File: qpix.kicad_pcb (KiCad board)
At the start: 4 copper layers, 82.6 x 92.8 mm, 110 parts, among them J1 Conn_01x40, J10 VC, J11 Conn_Coaxial_Power, J13 DigReset, J2 Conn_01x09, J3 Conn_02x03, J4 Conn_02x03, J5 SPI, J6 Conn_02x03, J7 Conn_Coaxial, J8 Conn_02x03, J9 Conn_Coaxial_Power, Q1 AO7400, Q2 AO7400, Q3 AO7400, Q4 AO7400, U1 qpix_digital, U2 TPS73101DBV, U3 9DMV0141AKILF, U4 DS90C401M_NOPB

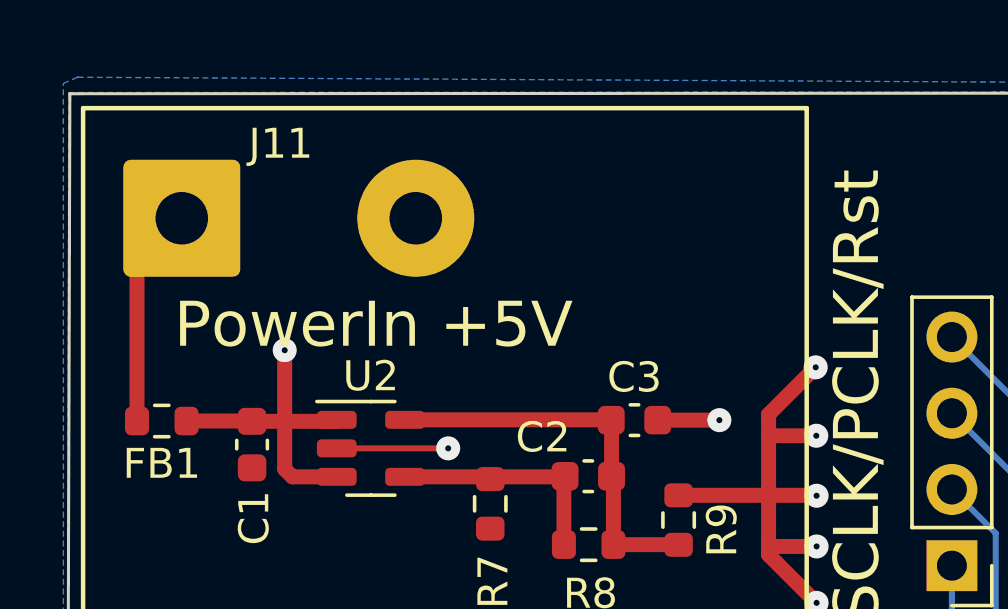
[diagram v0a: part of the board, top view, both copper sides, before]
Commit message: replace wire connector for 5V input with SMA conn
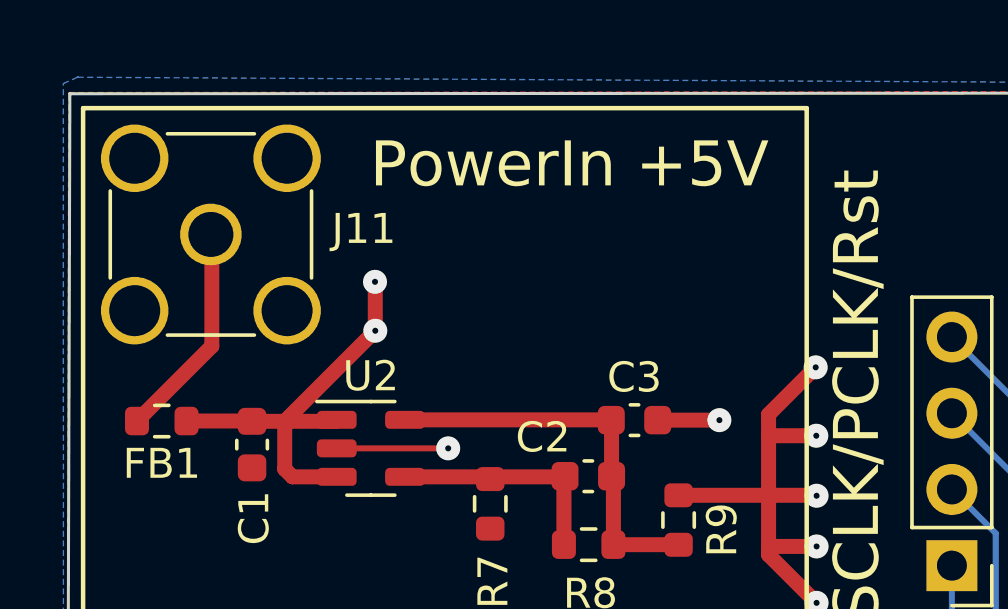
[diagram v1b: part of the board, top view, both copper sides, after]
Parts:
- J11: footprint Connector_Wire:SolderWire-1sqmm_1x02_P7.8mm_D1.4mm_OD3.9mm -> Connector_Coaxial:SMA_Amphenol_901-144_Vertical
- moved J11 1.11 mm to (100.2, 54.2)
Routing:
- net +5V: track 16.4 -> 19.9 mm, vias 5 -> 6
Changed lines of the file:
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@@
     )
   )
-  (footprint "Connector_Wire:SolderWire-1sqmm_1x02_P7.8mm_D1.4mm_OD3.9mm" (layer "F.Cu")
-    (at 99.26 53.62)
-    (descr "Soldered wire connection, for 2 times 1 mm² wires, reinforced insulation, conductor diameter 1.4mm, outer diameter 3.9mm, size source Multi-Contact FLEXI-xV 1.0 (https://ec.staubli.com/AcroFiles/Catalogues/TM_Cab-Main-11014119_(en)_hi.pdf), bend radius 3 times outer diameter, generated with kicad-footprint-generator")
-    (tags "connector wire 1sqmm")
+  (footprint "Connector_Coaxial:SMA_Amphenol_901-144_Vertical" (layer "F.Cu")
+    (at 100.23 54.16)
+    (descr "https://www.amphenolrf.com/downloads/dl/file/id/7023/product/3103/901_144_customer_drawing.pdf")
+    (tags "SMA THT Female Jack Vertical")
     (property "Sheetfile" "qpix-power.kicad_sch")
     (property "Sheetname" "qpix-power")
     (property "ki_description" "coaxial connector (BNC, SMA, SMB, SMC, Cinch/RCA, LEMO, ...)")
     (property "ki_keywords" "BNC SMA SMB SMC LEMO coaxial connector CINCH RCA")
-    (attr exclude_from_pos_files)
-    (fp_text reference "J11" (at 3.3 -2.48) (layer "F.SilkS")
+    (attr through_hole)
+    (fp_text reference "J11" (at 5.1 -0.18) (layer "F.SilkS")
         (effects (font (size 1 1) (thickness 0.15)))
     )
-    (fp_text value "Conn_Coaxial_Power" (at 3.9 3.15) (layer "F.Fab")
+    (fp_text value "Conn_Coaxial_Power" (at 0 5) (layer "F.Fab")
         (effects (font (size 1 1) (thickness 0.15)))
     )
-    (fp_text user "${REFERENCE}" (at 3.9 0 90) (layer "F.Fab")
+    (fp_text user "${REFERENCE}" (at 0 0) (layer "F.Fab")
         (effects (font (size 1 1) (thickness 0.15)))
     )
-    (fp_line (start -2.7 -2.45) (end -2.7 2.45)
-      (stroke (width 0.05) (type solid)) (layer "F.CrtYd"))
-    (fp_line (start -2.7 2.45) (end 2.7 2.45)
-      (stroke (width 0.05) (type solid)) (layer "F.CrtYd"))
-    (fp_line (start 2.7 -2.45) (end -2.7 -2.45)
-      (stroke (width 0.05) (type solid)) (layer "F.CrtYd"))
-    (fp_line (start 2.7 2.45) (end 2.7 -2.45)
-      (stroke (width 0.05) (type solid)) (layer "F.CrtYd"))
-    (fp_line (start 5.1 -2.45) (end 5.1 2.45)
+    (fp_line (start -3.355 -1.45) (end -3.355 1.45)
+      (stroke (width 0.12) (type solid)) (layer "F.SilkS"))
+    (fp_line (start -1.45 -3.355) (end 1.45 -3.355)
+      (stroke (width 0.12) (type solid)) (layer "F.SilkS"))
+    (fp_line (start -1.45 3.355) (end 1.45 3.355)
+      (stroke (width 0.12) (type solid)) (layer "F.SilkS"))
+    (fp_line (start 3.355 -1.45) (end 3.355 1.45)
+      (stroke (width 0.12) (type solid)) (layer "F.SilkS"))
+    (fp_line (start -4.17 -4.17) (end -4.17 4.17)
       (stroke (width 0.05) (type solid)) (layer "F.CrtYd"))
-    (fp_line (start 5.1 2.45) (end 10.5 2.45)
+    (fp_line (start -4.17 -4.17) (end 4.17 -4.17)
       (stroke (width 0.05) (type solid)) (layer "F.CrtYd"))
-    (fp_line (start 10.5 -2.45) (end 5.1 -2.45)
+    (fp_line (start 4.17 4.17) (end -4.17 4.17)
       (stroke (width 0.05) (type solid)) (layer "F.CrtYd"))
-    (fp_line (start 10.5 2.45) (end 10.5 -2.45)
+    (fp_line (start 4.17 4.17) (end 4.17 -4.17)
       (stroke (width 0.05) (type solid)) (layer "F.CrtYd"))
-    (fp_circle (center 0 0) (end 1.95 0)
-      (stroke (width 0.1) (type solid)) (fill none) (layer "F.Fab"))
-    (fp_circle (center 7.8 0) (end 9.75 0)
+    (fp_line (start -3.175 -3.175) (end -3.175 3.175)
+      (stroke (width 0.1) (type solid)) (layer "F.Fab"))
+    (fp_line (start -3.175 -3.175) (end 3.175 -3.175)
+      (stroke (width 0.1) (type solid)) (layer "F.Fab"))
+    (fp_line (start -3.175 3.175) (end 3.175 3.175)
+      (stroke (width 0.1) (type solid)) (layer "F.Fab"))
+    (fp_line (start 3.175 -3.175) (end 3.175 3.175)
+      (stroke (width 0.1) (type solid)) (layer "F.Fab"))
+    (fp_circle (center 0 0) (end 3.175 0)
       (stroke (width 0.1) (type solid)) (fill none) (layer "F.Fab"))
-    (pad "1" thru_hole roundrect (at 0 0) (size 3.9 3.9) (drill 1.75) (layers "*.Cu" "*.Mask") (roundrect_rratio 0.06410307692)
+    (pad "1" thru_hole circle (at 0 0) (size 2.05 2.05) (drill 1.5) (layers "*.Cu" "*.Mask")
       (net 71 "Net-(J11-In)") (pinfunction "In") (pintype "passive"))
-    (pad "2" thru_hole circle (at 7.8 0) (size 3.9 3.9) (drill 1.75) (layers "*.Cu" "*.Mask")
+    (pad "2" thru_hole circle (at -2.54 -2.54) (size 2.25 2.25) (drill 1.7) (layers "*.Cu" "*.Mask")
+      (net 80 "GND") (pinfunction "Ext") (pintype "passive"))
+    (pad "2" thru_hole circle (at -2.54 2.54) (size 2.25 2.25) (drill 1.7) (layers "*.Cu" "*.Mask")
+      (net 80 "GND") (pinfunction "Ext") (pintype "passive"))
+    (pad "2" thru_hole circle (at 2.54 -2.54) (size 2.25 2.25) (drill 1.7) (layers "*.Cu" "*.Mask")
+      (net 80 "GND") (pinfunction "Ext") (pintype "passive"))
+    (pad "2" thru_hole circle (at 2.54 2.54) (size 2.25 2.25) (drill 1.7) (layers "*.Cu" "*.Mask")
       (net 80 "GND") (pinfunction "Ext") (pintype "passive"))
-    (model "${KICAD6_3DMODEL_DIR}/Connector_Wire.3dshapes/SolderWire-1sqmm_1x02_P7.8mm_D1.4mm_OD3.9mm.wrl"
+    (model "${KICAD6_3DMODEL_DIR}/Connector_Coaxial.3dshapes/SMA_Amphenol_901-144_Vertical.wrl"
       (offset (xyz 0 0 0))
       (scale (xyz 1 1 1))
@@
     (effects (font (size 1 1) (thickness 0.15)))
   )
-  (gr_text "PowerIn +5V" (at 105.65 57.175) (layer "F.SilkS")
+  (gr_text "PowerIn +5V" (at 112.18 51.83) (layer "F.SilkS")
     (effects (font (size 1.5 1.5) (thickness 0.3)))
   )
@@
   (segment (start 158.28 138.09) (end 160.385 135.985) (width 0.2) (layer "F.Cu") (net 70))
   (segment (start 162.045 135.985) (end 162.99 135.985) (width 0.2) (layer "F.Cu") (net 70))
-  (segment (start 97.7675 55.1125) (end 97.7675 60.38) (width 0.5) (layer "F.Cu") (net 71))
-  (segment (start 99.26 53.62) (end 97.7675 55.1125) (width 0.5) (layer "F.Cu") (net 71))
+  (segment (start 100.26 57.8875) (end 97.7675 60.38) (width 0.5) (layer "F.Cu") (net 71))
+  (segment (start 100.26 54.19) (end 100.26 57.8875) (width 0.5) (layer "F.Cu") (net 71))
+  (segment (start 100.23 54.16) (end 100.26 54.19) (width 0.5) (layer "F.Cu") (net 71))
   (segment (start 172.079333 107.6875) (end 173.201833 107.6875) (width 0.2) (layer "F.Cu") (net 72))
   (segment (start 171.261833 106.87) (end 172.079333 107.6875) (width 0.2) (layer "F.Cu") (net 72))
@@
   (segment (start 147.505348 102.458135) (end 147.78 102.35) (width 0.11) (layer "F.Cu") (net 109))
   (segment (start 99.4175 60.38) (end 101.5925 60.38) (width 0.5) (layer "F.Cu") (net 110))
+  (segment (start 105.71 55.75) (end 105.7 55.74) (width 0.5) (layer "F.Cu") (net 110))
   (segment (start 102.69 60.39) (end 104.375 60.39) (width 0.5) (layer "F.Cu") (net 110))
+  (segment (start 105.71 57.37) (end 105.71 55.75) (width 0.5) (layer "F.Cu") (net 110))
   (segment (start 101.5925 60.38) (end 101.6025 60.39) (width 0.5) (layer "F.Cu") (net 110))
   (segment (start 101.6025 60.39) (end 102.69 60.39) (width 0.5) (layer "F.Cu") (net 110))
@@
   (segment (start 104.375 60.39) (end 104.425 60.34) (width 0.5) (layer "F.Cu") (net 110))
   (segment (start 174.911833 105.33) (end 176.301833 105.33) (width 0.2) (layer "F.Cu") (net 110))
+  (segment (start 105.71 57.37) (end 102.69 60.39) (width 0.5) (layer "F.Cu") (net 110))
   (segment (start 102.95 62.24) (end 102.69 61.98) (width 0.5) (layer "F.Cu") (net 110))
-  (segment (start 102.69 60.39) (end 102.69 58.02) (width 0.5) (layer "F.Cu") (net 110))
   (via micro (at 176.301833 111.08) (size 0.8) (drill 0.2) (layers "F.Cu" "In2.Cu") (net 110))
+  (via micro (at 105.7 55.74) (size 0.8) (drill 0.2) (layers "F.Cu" "In2.Cu") (net 110))
   (via micro (at 176.301833 105.33) (size 0.8) (drill 0.2) (layers "F.Cu" "In2.Cu") (net 110))
   (via micro (at 176.296833 122.54) (size 0.8) (drill 0.2) (layers "F.Cu" "In2.Cu") (net 110))
-  (via micro (at 102.69 58.02) (size 0.8) (drill 0.2) (layers "F.Cu" "In2.Cu") (net 110))
+  (via micro (at 105.71 57.37) (size 0.8) (drill 0.2) (layers "F.Cu" "In2.Cu") (net 110))
   (via micro (at 176.301833 116.82) (size 0.8) (drill 0.2) (layers "F.Cu" "In2.Cu") (net 110))
   (segment (start 149.805 66.112488) (end 149.805 63.032488) (width 0.2) (layer "F.Cu") (net 111))
@@
         (xy 177.39 50.1)
         (xy 177.39 124.49)
-        (xy 176.25 124.45)
-        (xy 176.63 51.1)
-        (xy 103.61 51.04)
-        (xy 103.62 58.77)
-        (xy 101.85 58.79)
-        (xy 101.91 50.21)
+        (xy 175.8 124.49)
+        (xy 176.04 51.82)
+        (xy 108.85 51.22)
+        (xy 108.83 58.67)
+        (xy 104.35 58.69)
+        (xy 104.41 50.11)
       )
     )

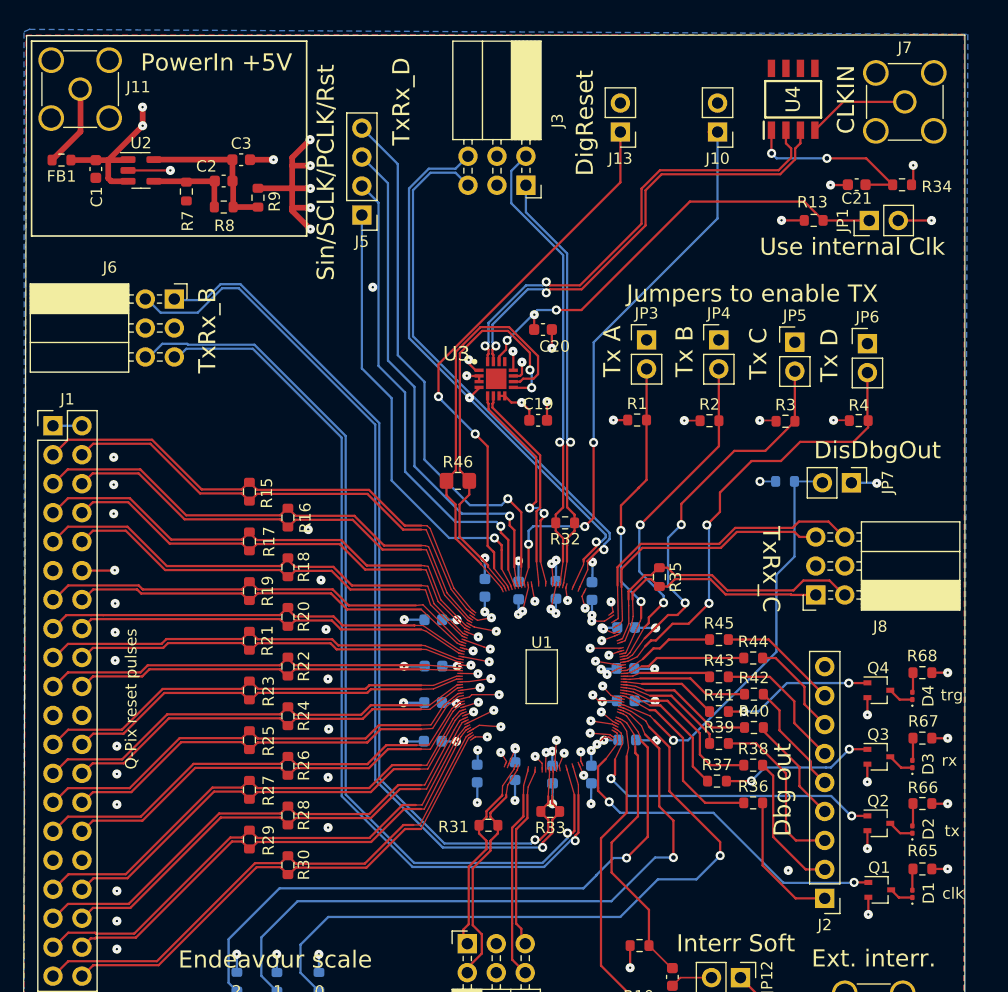
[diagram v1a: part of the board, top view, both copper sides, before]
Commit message: replace led footprints with 0603, add power up led
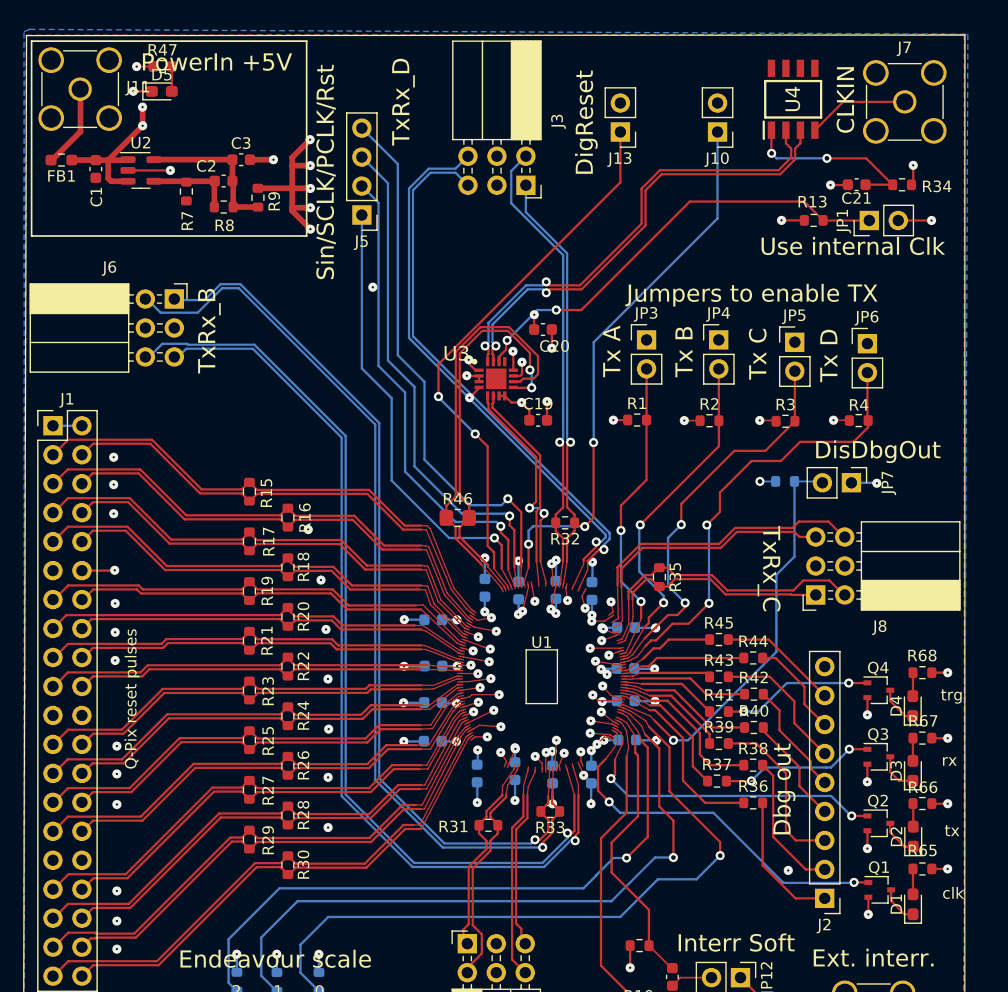
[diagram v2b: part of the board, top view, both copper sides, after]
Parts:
- added D5: LED, LED_SMD:LED_0603_1608Metric_Pad1.05x0.95mm_HandSolder, F.Cu at (107.4, 54.4)
- added R47: 220, Resistor_SMD:R_0603_1608Metric, F.Cu at (107.5, 52.2)
- D1, D2, D3, D4: footprint LED_SMD:LED_0201_0603Metric -> LED_SMD:LED_0603_1608Metric_Pad1.05x0.95mm_HandSolder
- FB1: footprint Resistor_SMD:R_0603_1608Metric -> Resistor_SMD:R_0603_1608Metric_Pad0.98x0.95mm_HandSolder
- moved R46 3.25 mm to (133.3, 91.8)
- moved D1 0.91 mm to (173.3, 125.6)
- moved D4 0.89 mm to (173.2, 108.3)
- moved D2 0.63 mm to (173.3, 119.7)
- moved D3 0.60 mm to (173.2, 113.9)
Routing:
- net Net-(D5-A): track 0.00 -> 2.18 mm
- net GND: track 104.7 -> 106.4 mm, vias 76 -> 77
- net +5V: track 19.9 -> 21.4 mm, vias 6 -> 7
- net Net-(D3-K): track 2.34 -> 3.65 mm
- net Net-(D1-K): track 2.14 -> 3.37 mm
- net Net-(D4-K): track 2.28 -> 3.47 mm
- net Net-(D2-K): track 2.30 -> 3.34 mm
